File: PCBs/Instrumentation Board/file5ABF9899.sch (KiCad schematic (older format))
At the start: 2 parts, among them J3 Conn_01x02

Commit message: swapped TX and RX pins
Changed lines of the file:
@@
 $Descr A4 11693 8268
 encoding utf-8
-Sheet 11 11
+Sheet 11 13
 Title ""
 Date ""
@@
 U 1 1 5ABF9936
 P 4750 2750
+AR Path="/5ABF989A/5ABF9936" Ref="#PWR43"  Part="1"
+AR Path="/5ABFB303/5ABF9936" Ref="#PWR45"  Part="1"
+AR Path="/5ABFB538/5ABF9936" Ref="#PWR47"  Part="1"
 F 0 "#PWR43" H 4750 2600 50  0001 C CNN
 F 1 "+5V" H 4750 2890 50  0000 C CNN
@@
 U 1 1 5ABF994A
 P 4750 3000
+AR Path="/5ABF989A/5ABF994A" Ref="R4"  Part="1"
+AR Path="/5ABFB303/5ABF994A" Ref="R5"  Part="1"
+AR Path="/5ABFB538/5ABF994A" Ref="R6"  Part="1"
 F 0 "R4" V 4830 3000 50  0000 C CNN
 F 1 "R" V 4750 3000 50  0000 C CNN
@@
 U 1 1 5ABF9969
 P 4850 3700
+AR Path="/5ABF989A/5ABF9969" Ref="J3"  Part="1"
+AR Path="/5ABFB303/5ABF9969" Ref="J4"  Part="1"
+AR Path="/5ABFB538/5ABF9969" Ref="J5"  Part="1"
 F 0 "J3" H 4850 3800 50  0000 C CNN
 F 1 "Conn_01x02" H 4850 3500 50  0000 C CNN
@@
 U 1 1 5ABF9996
 P 5400 3500
+AR Path="/5ABF989A/5ABF9996" Ref="#PWR44"  Part="1"
+AR Path="/5ABFB303/5ABF9996" Ref="#PWR46"  Part="1"
+AR Path="/5ABFB538/5ABF9996" Ref="#PWR48"  Part="1"
 F 0 "#PWR44" H 5400 3250 50  0001 C CNN
 F 1 "GND" H 5400 3350 50  0000 C CNN
@@
 	5400 3400 5400 3500
 Wire Wire Line
-	4750 3500 4750 3300
-Wire Wire Line
-	4750 3300 4750 3150
+	4750 3150 4750 3500
 Wire Wire Line
 	4750 2850 4750 2750

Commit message: Fixed weird merge issue (2)
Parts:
- J3: footprint (none) -> molex:molex_kk_22-23-2021
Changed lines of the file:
@@
 F 0 "J3" H 4850 3800 50  0000 C CNN
 F 1 "Conn_01x02" H 4850 3500 50  0000 C CNN
-F 2 "" H 4850 3700 50  0001 C CNN
+F 2 "molex:molex_kk_22-23-2021" H 4850 3700 50  0001 C CNN
 F 3 "" H 4850 3700 50  0001 C CNN
 	1    4850 3700

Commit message: review changes + instr board PCB
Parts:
- R4: footprint (none) -> Resistors_SMD:R_0805_HandSoldering
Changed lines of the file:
@@
 $EndDescr
 $Comp
-L +5V #PWR43
+L +5V #PWR043
 U 1 1 5ABF9936
 P 4750 2750
-AR Path="/5ABF989A/5ABF9936" Ref="#PWR43"  Part="1"
-AR Path="/5ABFB303/5ABF9936" Ref="#PWR45"  Part="1"
-AR Path="/5ABFB538/5ABF9936" Ref="#PWR47"  Part="1"
-F 0 "#PWR43" H 4750 2600 50  0001 C CNN
+AR Path="/5ABF989A/5ABF9936" Ref="#PWR043"  Part="1"
+AR Path="/5ABFB303/5ABF9936" Ref="#PWR045"  Part="1"
+AR Path="/5ABFB538/5ABF9936" Ref="#PWR047"  Part="1"
+F 0 "#PWR047" H 4750 2600 50  0001 C CNN
 F 1 "+5V" H 4750 2890 50  0000 C CNN
 F 2 "" H 4750 2750 50  0001 C CNN
@@
 AR Path="/5ABFB303/5ABF994A" Ref="R5"  Part="1"
 AR Path="/5ABFB538/5ABF994A" Ref="R6"  Part="1"
-F 0 "R4" V 4830 3000 50  0000 C CNN
+F 0 "R6" V 4830 3000 50  0000 C CNN
 F 1 "R" V 4750 3000 50  0000 C CNN
-F 2 "" V 4680 3000 50  0001 C CNN
+F 2 "Resistors_SMD:R_0805_HandSoldering" V 4680 3000 50  0001 C CNN
 F 3 "" H 4750 3000 50  0001 C CNN
 	1    4750 3000
@@
 AR Path="/5ABFB303/5ABF9969" Ref="J4"  Part="1"
 AR Path="/5ABFB538/5ABF9969" Ref="J5"  Part="1"
-F 0 "J3" H 4850 3800 50  0000 C CNN
+F 0 "J5" H 4850 3800 50  0000 C CNN
 F 1 "Conn_01x02" H 4850 3500 50  0000 C CNN
 F 2 "molex:molex_kk_22-23-2021" H 4850 3700 50  0001 C CNN
@@
 $EndComp
 $Comp
-L GND #PWR44
+L GND #PWR044
 U 1 1 5ABF9996
 P 5400 3500
-AR Path="/5ABF989A/5ABF9996" Ref="#PWR44"  Part="1"
-AR Path="/5ABFB303/5ABF9996" Ref="#PWR46"  Part="1"
-AR Path="/5ABFB538/5ABF9996" Ref="#PWR48"  Part="1"
-F 0 "#PWR44" H 5400 3250 50  0001 C CNN
+AR Path="/5ABF989A/5ABF9996" Ref="#PWR044"  Part="1"
+AR Path="/5ABFB303/5ABF9996" Ref="#PWR046"  Part="1"
+AR Path="/5ABFB538/5ABF9996" Ref="#PWR048"  Part="1"
+F 0 "#PWR048" H 5400 3250 50  0001 C CNN
 F 1 "GND" H 5400 3350 50  0000 C CNN
 F 2 "" H 5400 3500 50  0001 C CNN

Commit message: finished traces on instr board
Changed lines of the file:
@@
 AR Path="/5ABFB303/5ABF9936" Ref="#PWR045"  Part="1"
 AR Path="/5ABFB538/5ABF9936" Ref="#PWR047"  Part="1"
-F 0 "#PWR047" H 4750 2600 50  0001 C CNN
+F 0 "#PWR043" H 4750 2600 50  0001 C CNN
 F 1 "+5V" H 4750 2890 50  0000 C CNN
 F 2 "" H 4750 2750 50  0001 C CNN
@@
 AR Path="/5ABFB303/5ABF994A" Ref="R5"  Part="1"
 AR Path="/5ABFB538/5ABF994A" Ref="R6"  Part="1"
-F 0 "R6" V 4830 3000 50  0000 C CNN
+F 0 "R4" V 4830 3000 50  0000 C CNN
 F 1 "R" V 4750 3000 50  0000 C CNN
 F 2 "Resistors_SMD:R_0805_HandSoldering" V 4680 3000 50  0001 C CNN
@@
 AR Path="/5ABFB303/5ABF9969" Ref="J4"  Part="1"
 AR Path="/5ABFB538/5ABF9969" Ref="J5"  Part="1"
-F 0 "J5" H 4850 3800 50  0000 C CNN
+F 0 "J3" H 4850 3800 50  0000 C CNN
 F 1 "Conn_01x02" H 4850 3500 50  0000 C CNN
 F 2 "molex:molex_kk_22-23-2021" H 4850 3700 50  0001 C CNN
@@
 AR Path="/5ABFB303/5ABF9996" Ref="#PWR046"  Part="1"
 AR Path="/5ABFB538/5ABF9996" Ref="#PWR048"  Part="1"
-F 0 "#PWR048" H 5400 3250 50  0001 C CNN
+F 0 "#PWR044" H 5400 3250 50  0001 C CNN
 F 1 "GND" H 5400 3350 50  0000 C CNN
 F 2 "" H 5400 3500 50  0001 C CNN

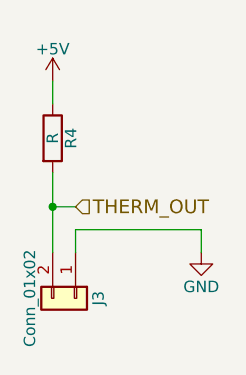
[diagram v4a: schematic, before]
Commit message: rerouted payload instr board and completed all changes per Alexs review
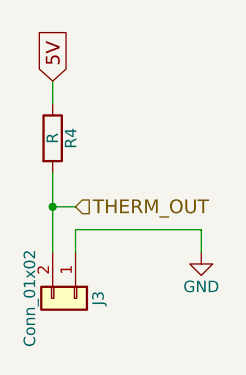
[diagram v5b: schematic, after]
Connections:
- net +5V renamed 5V
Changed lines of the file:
@@
 $EndDescr
-$Comp
-L +5V #PWR043
-U 1 1 5ABF9936
-P 4750 2750
-AR Path="/5ABF989A/5ABF9936" Ref="#PWR043"  Part="1"
-AR Path="/5ABFB303/5ABF9936" Ref="#PWR045"  Part="1"
-AR Path="/5ABFB538/5ABF9936" Ref="#PWR047"  Part="1"
-F 0 "#PWR043" H 4750 2600 50  0001 C CNN
-F 1 "+5V" H 4750 2890 50  0000 C CNN
-F 2 "" H 4750 2750 50  0001 C CNN
-F 3 "" H 4750 2750 50  0001 C CNN
-	1    4750 2750
-	1    0    0    -1
-$EndComp
 $Comp
 L R R4
@@
 $EndComp
 $Comp
-L GND #PWR044
+L GND #PWR042
 U 1 1 5ABF9996
 P 5400 3500
-AR Path="/5ABF989A/5ABF9996" Ref="#PWR044"  Part="1"
-AR Path="/5ABFB303/5ABF9996" Ref="#PWR046"  Part="1"
-AR Path="/5ABFB538/5ABF9996" Ref="#PWR048"  Part="1"
-F 0 "#PWR044" H 5400 3250 50  0001 C CNN
+AR Path="/5ABF989A/5ABF9996" Ref="#PWR042"  Part="1"
+AR Path="/5ABFB303/5ABF9996" Ref="#PWR044"  Part="1"
+AR Path="/5ABFB538/5ABF9996" Ref="#PWR046"  Part="1"
+F 0 "#PWR042" H 5400 3250 50  0001 C CNN
 F 1 "GND" H 5400 3350 50  0000 C CNN
 F 2 "" H 5400 3500 50  0001 C CNN
@@
 	4750 3300 4850 3300
 Connection ~ 4750 3300
+Text GLabel 4750 2750 1    60   Input ~ 0
+5V
 $EndSCHEMATC

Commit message: Fixed instr and recovery components per Alexs review
Added IMU current limiting resistors
Moved the caps near J4 on instr
Swapped out phototransistor footprint
Flipped I2C silk screen on J1 recovery
Flipped GND and TX silk screen on J6 recovery
renamed strat to alt on recovery silk screen
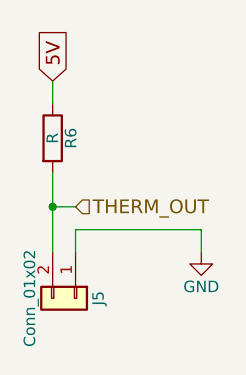
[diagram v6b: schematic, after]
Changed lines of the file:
@@
 AR Path="/5ABFB303/5ABF994A" Ref="R5"  Part="1"
 AR Path="/5ABFB538/5ABF994A" Ref="R6"  Part="1"
-F 0 "R4" V 4830 3000 50  0000 C CNN
+F 0 "R6" V 4830 3000 50  0000 C CNN
 F 1 "R" V 4750 3000 50  0000 C CNN
 F 2 "Resistors_SMD:R_0805_HandSoldering" V 4680 3000 50  0001 C CNN
@@
 AR Path="/5ABFB303/5ABF9969" Ref="J4"  Part="1"
 AR Path="/5ABFB538/5ABF9969" Ref="J5"  Part="1"
-F 0 "J3" H 4850 3800 50  0000 C CNN
+F 0 "J5" H 4850 3800 50  0000 C CNN
 F 1 "Conn_01x02" H 4850 3500 50  0000 C CNN
 F 2 "molex:molex_kk_22-23-2021" H 4850 3700 50  0001 C CNN
@@
 $EndComp
 $Comp
-L GND #PWR042
+L GND #PWR041
 U 1 1 5ABF9996
 P 5400 3500
-AR Path="/5ABF989A/5ABF9996" Ref="#PWR042"  Part="1"
-AR Path="/5ABFB303/5ABF9996" Ref="#PWR044"  Part="1"
-AR Path="/5ABFB538/5ABF9996" Ref="#PWR046"  Part="1"
-F 0 "#PWR042" H 5400 3250 50  0001 C CNN
+AR Path="/5ABF989A/5ABF9996" Ref="#PWR041"  Part="1"
+AR Path="/5ABFB303/5ABF9996" Ref="#PWR042"  Part="1"
+AR Path="/5ABFB538/5ABF9996" Ref="#PWR043"  Part="1"
+F 0 "#PWR043" H 5400 3250 50  0001 C CNN
 F 1 "GND" H 5400 3350 50  0000 C CNN
 F 2 "" H 5400 3500 50  0001 C CNN
